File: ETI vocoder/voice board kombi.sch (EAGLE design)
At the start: 94 parts, among them IC1 TL072P, IC2 TL072P, IC3 TL081P, IC4 TL081P, IC5 TL072P, IC6 LM13600AN, IC7 TL072P, Q1 BF244, Q2 BC214

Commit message: Duplicated all parts, ready for creating channel 2 (after main computer bailed on me and I lost a days work)
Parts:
- added C1., C10., C11., C12., C2., C3., C4., C5., C6., C7., C8., C9., CE1., CE2., CE3., CE4.: (no value), resistor:C-EU050-025X075
- added D1., D2., D3., D4.: (no value), diode:DIODE-D-5
- added IC1., IC2., IC7.: TL072P, linear:TL072P
- added IC3., IC4.: TL081P, linear:TL081P
- added PR1., PR2., PR3., PR4., PR5.: (no value), pot:TRIM_EU-CA9V
- added Q1.: BF244, transistor-fet:TN0602N3
- added Q2.: BC214, transistor-pnp:BC214
- added R1., R10., R11., R12., R13., R14., R15., R16., R17., R18., R19., R2., R20., R21., R22., R23., R24., R25., R26., R27., R28., R29., R3., R30., R31., R32., R33., R34., R4., R5., R6., R7., R8., R9., RE1., RE10., RE2., RE3., RE4., RE5., RE6., RE7.: (no value), resistor:R-US_0207/7
- added RV1.: 100k log, joakim:POT16_W_BRACKET""
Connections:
- new net BIAS2: R16..1, R33..1, R34..2
- new net N$47: C1..2, IC1.A.-IN, R2..1, RE3..2
- new net N$48: C1..1, C2..1, PR1..A, R1..2, RE2..1
- new net N$49: C2..2, IC1.A.OUT, R2..2, R3..1
- new net N$50: C3..1, C4..1, R3..2, R4..2, RE4..1
- new net N$51: C3..2, IC1.B.-IN, R5..2
- new net N$52: IC1.B.+IN, R6..2, RE4..2
- new net N$53: C4..2, IC1.B.OUT, R5..1, R7..1
- new net N$54: IC2.B.-IN, R7..2, R8..1, R9..1
- new net N$55: D1..C, IC2.A.+IN, R8..2
- new net N$56: D1..A, D2..C, IC2.B.OUT
- new net N$57: D2..A, R10..1, R9..2
- new net N$58: IC2.A.-IN, R10..2, R11..1
- new net N$59: IC2.A.OUT, R11..2, R12..1
- new net N$60: C5..2, R12..2, R13..1
- new net N$61: C5..1, IC3..-IN, IC3..OUT, R14..1, R15..2
- new net N$62: C6..2, IC3..+IN, R13..2
- new net N$63: Q1..D, R15..1, R16..2
- new net N$64: C7..2, IC4..+IN, Q1..S
- new net N$65: D3..A, Q1..G, R17..2
- new net N$66: IC4..-IN, IC4..OUT, IC5B.+IN, R17..1
- new net N$67: D4..C, IC5B.-IN, R18..1
- new net N$68: D4..A, IC5B.OUT, PR2..E
- new net N$69: PR2..A, PR2..S, Q2..E, R19..1
- new net N$70: PR3..S, R19..2
- new net N$71: Q2..C, R20..2
- new net N$72: PR4..A, R31..2
- new net N$73: C8..2, C9..2, PR5..A, R21..2, RE5..1
- new net N$74: C10..2, C11..2, R23..2, R24..2, RE7..1
- new net N$75: C8..1, IC7.A.-IN, R22..1, RE10..2
- new net N$76: C9..1, IC7.A.OUT, R22..2, R23..1
- new net N$77: C11..1, IC7.B.OUT, R25..2, R27..1
- new net N$78: PR4..E, R32..1
- new net N$79: IC6B.+IN, R32..2
- new net N$80: IC6B.DIODE/BIAS, R28..1
- new net N$81: IC6B.-IN, R27..2, R31..1
- new net N$82: IC6B.AMP/BIAS, R20..1
- new net N$83: IC6B.BUFF/IN, RV1.G$1.1S
- new net N$84: C12..2, IC6B.BUFF/OUT, R29..1
- new net N$85: C12..1, R30..1
- new net N$86: C10..1, IC7.B.-IN, R25..1
- new net N$87: IC7.B.+IN, R26..2, RE7..2
- new net N$88: CE1..2, R1..1, RE1..2
- new net N$89: CE2..2, IC1.A.+IN, RE2..2
- new net N$90: CE3..2, R21..1
- new net N$91: CE4..2, IC7.A.+IN, RE5..2, RE6..2
- new net N$92: IC6B.OUT, RV1.G$1.1E
- net +12V: now also IC1.P.V+, IC2.P.V+, IC3..V+, IC4..V+, IC7.P.V+, PR3..A, R28..2, R33..2
- net -12V: now also IC1.P.V-, IC2.P.V-, IC3..V-, IC4..V-, IC7.P.V-, PR3..E, R29..2
- net EXITATION_IN: now also CE3..1
- net GND: now also C6..1, C7..1, CE2..1, CE4..1, IC2.B.+IN, PR1..E, PR1..S, PR4..S, PR5..E, PR5..S, Q2..B, R18..2, R24..1, R26..1, R34..1, R4..1, R6..1, RE1..1, RE10..1, RE3..1, RE6..1, RV1.G$1.1A
- net OUTPUT_AMP: now also R30..2
- net SLEW_RATE_CTRL: now also D3..C
- net SPEECH_IN: now also CE1..1
- net VU_DETECTOR: now also R14..2
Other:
- moved on the sheet: C12, C5, C6, C7, CE1, CE2, CE3, CE4, D1, D2, D3, D4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

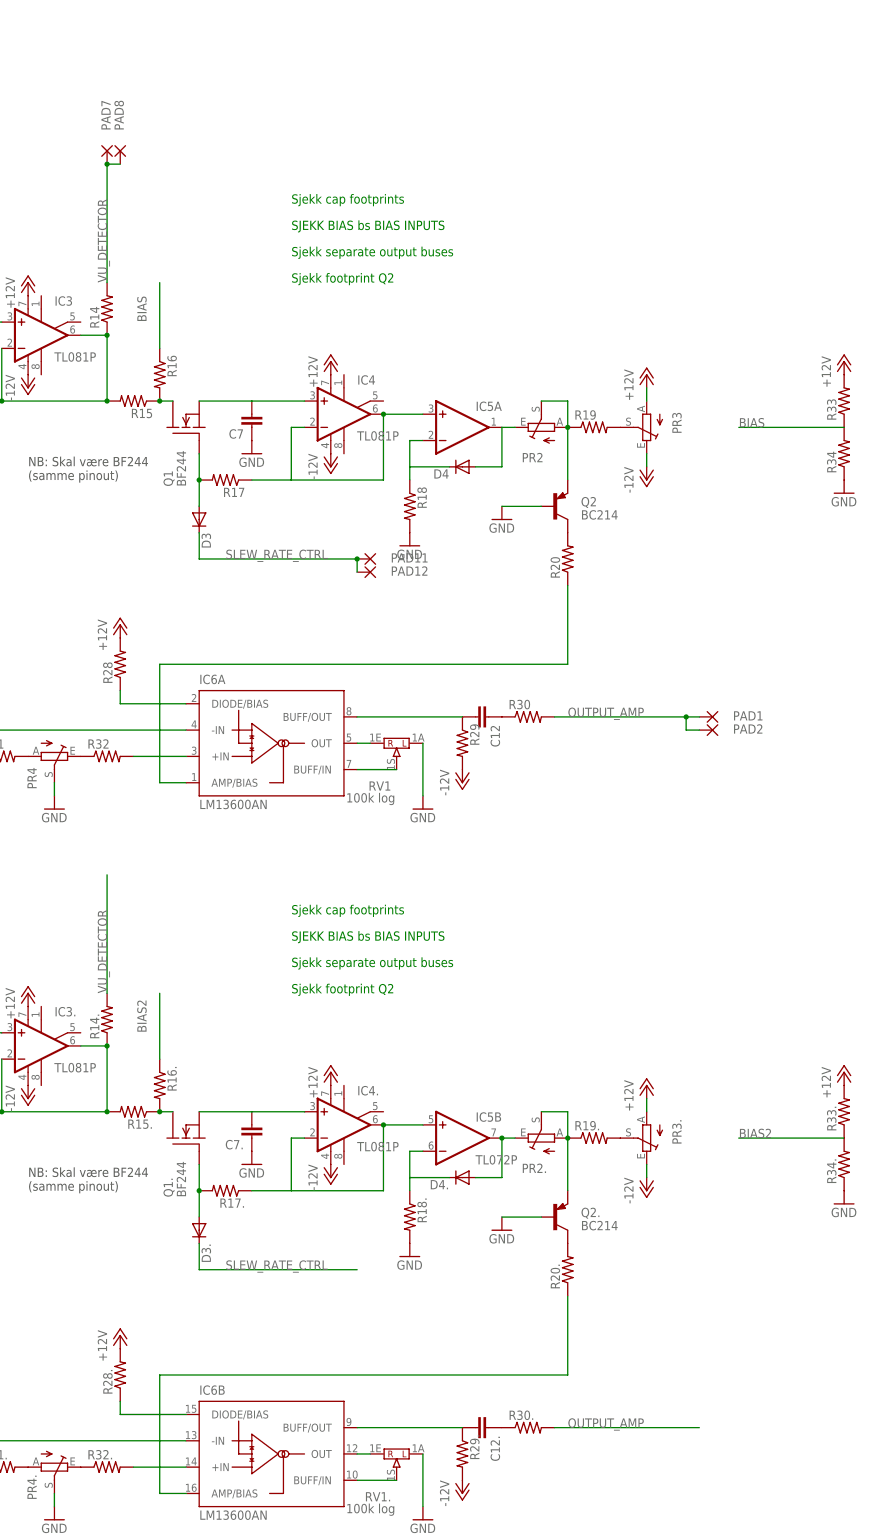
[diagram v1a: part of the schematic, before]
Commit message: Checked and fixed Q2, still need to check cap footprints and shrink board
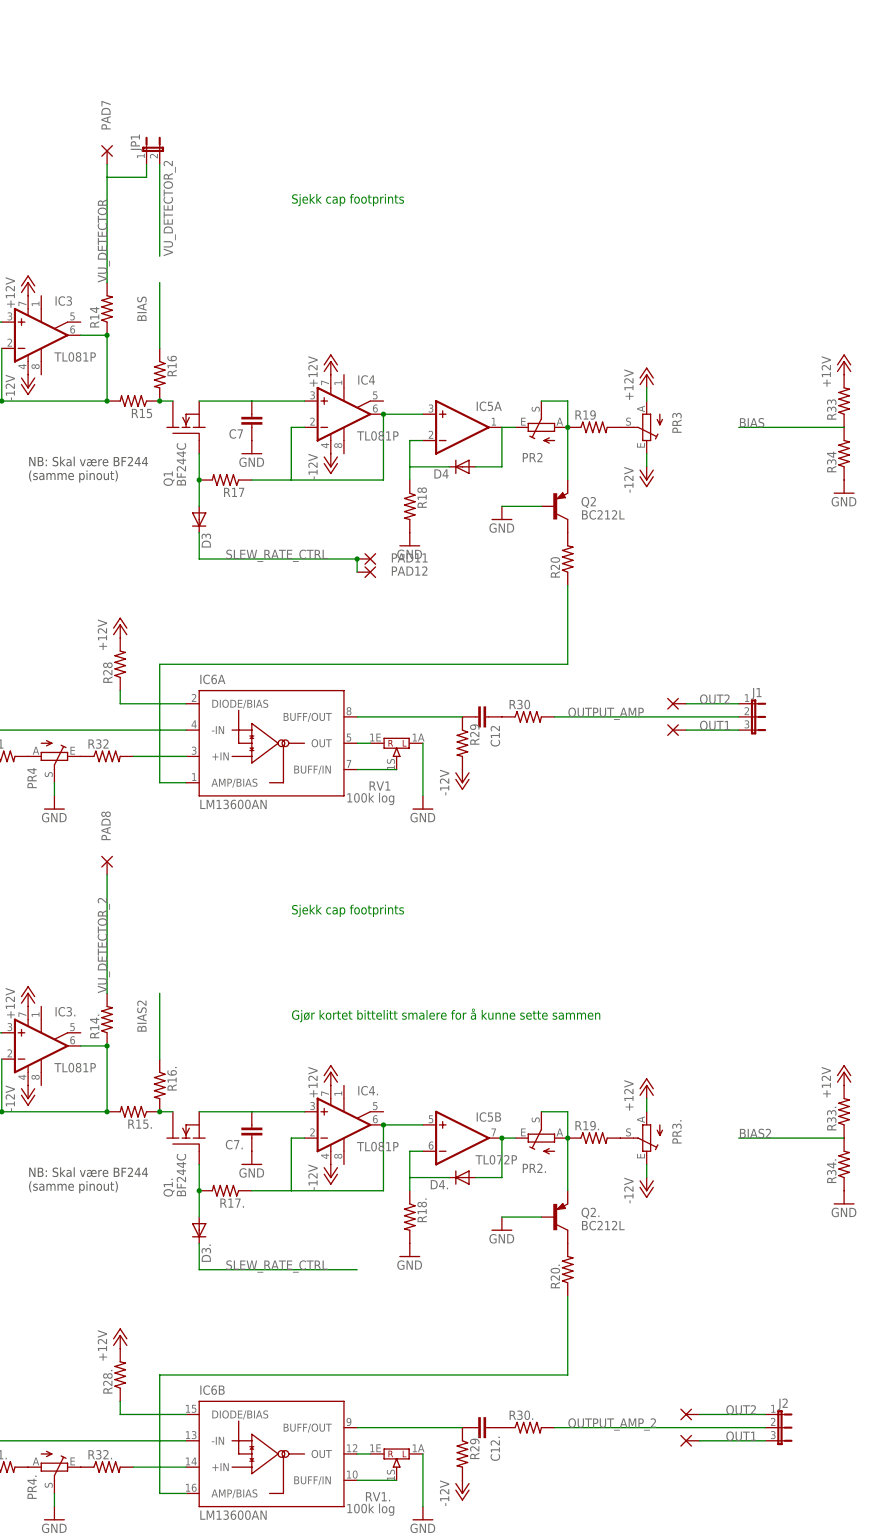
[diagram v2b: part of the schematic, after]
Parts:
- added J1, J2: (no value), jumper:JP2E
- added JP1: (no value), jumper:JP1E
- added PAD17, PAD18: WIREPAD2,54/1,1, wirepad:WIREPAD2,54/1,1
- Q1, Q1.: value BF244 -> BF244C
- Q2, Q2.: value BC214 -> BC212L; device transistor-pnp:BC214 -> transistor-neu-to92:-PNP-TO92-ECB
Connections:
- new net OUT1: J1.3, J2.3, PAD1.P, PAD2.P
- new net OUT2: J1.1, J2.1, PAD17.P, PAD18.P
- new net OUTPUT_AMP_2: J2.2, R30..2
- new net VU_DETECTOR_2: JP1.2, PAD8.P, R14..2
- net OUTPUT_AMP: now also J1.2; no longer PAD1.P, PAD2.P, R30..2
- net VU_DETECTOR: now also JP1.1; no longer PAD8.P, R14..2
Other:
- note added: "Gjør kortet bittelitt smalere for å kunne sette sammen"
- note removed: "SJEKK BIAS bs BIAS INPUTS"
- note removed: "Sjekk footprint Q2"
- note removed: "Sjekk separate output buses"
- moved on the sheet: PAD8
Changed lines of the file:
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@@
 <part name="C6" library="resistor" deviceset="C-EU" device="050-025X075"/>
 <part name="GND5" library="supply1" deviceset="GND" device=""/>
-<part name="Q1" library="transistor-fet" deviceset="TN0602N3" device="" value="BF244"/>
+<part name="Q1" library="transistor-fet" deviceset="TN0602N3" device="" value="BF244C"/>
 <part name="D3" library="diode" deviceset="DIODE-" device="D-5"/>
 <part name="R17" library="resistor" deviceset="R-US_" device="0207/7"/>
@@
 <part name="P+1" library="supply1" deviceset="+12V" device=""/>
 <part name="P-1" library="supply1" deviceset="-12V" device=""/>
-<part name="Q2" library="transistor-pnp" deviceset="BC214" device=""/>
+<part name="Q2" library="transistor-neu-to92" deviceset="*-PNP-" device="TO92-ECB" value="BC212L"/>
 <part name="GND8" library="supply1" deviceset="GND" device=""/>
 <part name="R20" library="resistor" deviceset="R-US_" device="0207/7"/>
@@
 <part name="C6." library="resistor" deviceset="C-EU" device="050-025X075"/>
 <part name="GND27" library="supply1" deviceset="GND" device=""/>
-<part name="Q1." library="transistor-fet" deviceset="TN0602N3" device="" value="BF244"/>
+<part name="Q1." library="transistor-fet" deviceset="TN0602N3" device="" value="BF244C"/>
 <part name="D3." library="diode" deviceset="DIODE-" device="D-5"/>
 <part name="R17." library="resistor" deviceset="R-US_" device="0207/7"/>
@@
 <part name="P+9" library="supply1" deviceset="+12V" device=""/>
 <part name="P-8" library="supply1" deviceset="-12V" device=""/>
-<part name="Q2." library="transistor-pnp" deviceset="BC214" device=""/>
+<part name="Q2." library="transistor-neu-to92" deviceset="*-PNP-" device="TO92-ECB" value="BC212L"/>
 <part name="GND30" library="supply1" deviceset="GND" device=""/>
 <part name="R20." library="resistor" deviceset="R-US_" device="0207/7"/>
@@
 <part name="P-12" library="supply1" deviceset="-12V" device=""/>
 <part name="P+14" library="supply1" deviceset="+12V" device=""/>
+<part name="J1" library="jumper" deviceset="JP2E" device=""/>
+<part name="J2" library="jumper" deviceset="JP2E" device=""/>
+<part name="PAD17" library="wirepad" deviceset="WIREPAD" device="2,54/1,1"/>
+<part name="PAD18" library="wirepad" deviceset="WIREPAD" device="2,54/1,1"/>
+<part name="JP1" library="jumper" deviceset="JP1E" device=""/>
 </parts>
 <sheets>
@@
 H: R24
 L: R24</text>
-<text x="233.68" y="231.14" size="1.778" layer="91">SJEKK BIAS bs BIAS INPUTS</text>
-<text x="233.68" y="226.06" size="1.778" layer="91">Sjekk separate output buses</text>
 <text x="233.68" y="236.22" size="1.778" layer="91">Sjekk cap footprints</text>
-<text x="233.68" y="220.98" size="1.778" layer="91">Sjekk footprint Q2</text>
 <text x="111.76" y="185.42" size="1.778" layer="97">2A and 2B are switched in the article</text>
 <text x="182.88" y="45.72" size="1.778" layer="97">NB: Skal være BF244
@@
 H: R24
 L: R24</text>
-<text x="233.68" y="93.98" size="1.778" layer="91">SJEKK BIAS bs BIAS INPUTS</text>
-<text x="233.68" y="88.9" size="1.778" layer="91">Sjekk separate output buses</text>
 <text x="233.68" y="99.06" size="1.778" layer="91">Sjekk cap footprints</text>
-<text x="233.68" y="83.82" size="1.778" layer="91">Sjekk footprint Q2</text>
 <text x="111.76" y="48.26" size="1.778" layer="97">2A and 2B are switched in the article</text>
+<text x="233.68" y="78.74" size="1.778" layer="91">Gjør kortet bittelitt smalere for å kunne sette sammen</text>
 </plain>
 <instances>
@@
 <instance part="P-6" gate="1" x="114.3" y="238.76"/>
 <instance part="P+7" gate="1" x="114.3" y="259.08"/>
-<instance part="PAD1" gate="G$1" x="314.96" y="137.16" smashed="yes" rot="R180">
-<attribute name="NAME" x="318.897" y="136.4742" size="1.778" layer="95"/>
-</instance>
-<instance part="PAD2" gate="G$1" x="314.96" y="134.62" smashed="yes" rot="R180">
-<attribute name="NAME" x="318.897" y="133.9342" size="1.778" layer="95"/>
-</instance>
+<instance part="PAD1" gate="G$1" x="307.34" y="134.62" smashed="yes"/>
+<instance part="PAD2" gate="G$1" x="309.88" y="-2.54" smashed="yes"/>
 <instance part="PAD3" gate="G$1" x="33.02" y="137.16" smashed="yes">
 <attribute name="NAME" x="29.083" y="137.8458" size="1.778" layer="95" rot="R180"/>
@@
 <attribute name="NAME" x="198.8058" y="250.317" size="1.778" layer="95" rot="R90"/>
 </instance>
-<instance part="PAD8" gate="G$1" x="200.66" y="246.38" smashed="yes" rot="R270">
-<attribute name="NAME" x="201.3458" y="250.317" size="1.778" layer="95" rot="R90"/>
+<instance part="PAD8" gate="G$1" x="198.12" y="109.22" smashed="yes" rot="R270">
+<attribute name="NAME" x="198.8058" y="113.157" size="1.778" layer="95" rot="R90"/>
 </instance>
 <instance part="PAD11" gate="G$1" x="248.92" y="167.64" smashed="yes" rot="R180">
@@
 <instance part="P+14" gate="1" x="114.3" y="114.3"/>
 <instance part="IC5" gate="B" x="266.7" y="55.88"/>
+<instance part="J1" gate="1" x="322.58" y="137.16" rot="R270"/>
+<instance part="J2" gate="1" x="327.66" y="0" rot="R270"/>
+<instance part="PAD17" gate="G$1" x="307.34" y="139.7" smashed="yes"/>
+<instance part="PAD18" gate="G$1" x="309.88" y="2.54" smashed="yes"/>
+<instance part="JP1" gate="A" x="205.74" y="246.38"/>
 </instances>
 <busses>
@@
 <segment>
 <pinref part="R14" gate="G$1" pin="2"/>
-<wire x1="198.12" y1="220.98" x2="198.12" y2="243.84" width="0.1524" layer="91"/>
+<wire x1="198.12" y1="220.98" x2="198.12" y2="241.3" width="0.1524" layer="91"/>
 <label x="198.12" y="220.98" size="1.778" layer="95" rot="R90"/>
-<pinref part="PAD8" gate="G$1" pin="P"/>
 <pinref part="PAD7" gate="G$1" pin="P"/>
-<wire x1="200.66" y1="243.84" x2="198.12" y2="243.84" width="0.1524" layer="91"/>
-<junction x="198.12" y="243.84"/>
-</segment>
-<segment>
-<pinref part="R14." gate="G$1" pin="2"/>
-<wire x1="198.12" y1="83.82" x2="198.12" y2="106.68" width="0.1524" layer="91"/>
-<label x="198.12" y="83.82" size="1.778" layer="95" rot="R90"/>
+<wire x1="198.12" y1="241.3" x2="198.12" y2="243.84" width="0.1524" layer="91"/>
+<wire x1="198.12" y1="241.3" x2="205.74" y2="241.3" width="0.1524" layer="91"/>
+<pinref part="JP1" gate="A" pin="1"/>
+<wire x1="205.74" y1="241.3" x2="205.74" y2="243.84" width="0.1524" layer="91"/>
 </segment>
 </net>
@@
 <segment>
 <pinref part="R30" gate="G$1" pin="2"/>
-<wire x1="284.48" y1="137.16" x2="309.88" y2="137.16" width="0.1524" layer="91"/>
+<wire x1="284.48" y1="137.16" x2="320.04" y2="137.16" width="0.1524" layer="91"/>
 <label x="287.02" y="137.16" size="1.778" layer="95"/>
-<pinref part="PAD1" gate="G$1" pin="P"/>
-<pinref part="PAD2" gate="G$1" pin="P"/>
-<wire x1="309.88" y1="137.16" x2="312.42" y2="137.16" width="0.1524" layer="91"/>
-<wire x1="312.42" y1="134.62" x2="309.88" y2="134.62" width="0.1524" layer="91"/>
-<wire x1="309.88" y1="134.62" x2="309.88" y2="137.16" width="0.1524" layer="91"/>
-<junction x="309.88" y="137.16"/>
-</segment>
-<segment>
-<pinref part="R30." gate="G$1" pin="2"/>
-<wire x1="284.48" y1="0" x2="312.42" y2="0" width="0.1524" layer="91"/>
-<label x="287.02" y="0" size="1.778" layer="95"/>
+<pinref part="J1" gate="1" pin="2"/>
 </segment>
 </net>
@@
 </segment>
 </net>
+<net name="OUT1" class="0">
+<segment>
+<pinref part="J2" gate="1" pin="3"/>
+<pinref part="PAD2" gate="G$1" pin="P"/>
+<wire x1="312.42" y1="-2.54" x2="325.12" y2="-2.54" width="0.1524" layer="91"/>
+<label x="317.5" y="-2.54" size="1.778" layer="95"/>
+</segment>
+<segment>
+<pinref part="J1" gate="1" pin="3"/>
+<pinref part="PAD1" gate="G$1" pin="P"/>
+<wire x1="309.88" y1="134.62" x2="320.04" y2="134.62" width="0.1524" layer="91"/>
+<label x="312.42" y="134.62" size="1.778" layer="95"/>
+</segment>
+</net>
+<net name="OUT2" class="0">
+<segment>
+<pinref part="J2" gate="1" pin="1"/>
+<pinref part="PAD18" gate="G$1" pin="P"/>
+<wire x1="312.42" y1="2.54" x2="325.12" y2="2.54" width="0.1524" layer="91"/>
+<label x="317.5" y="2.54" size="1.778" layer="95"/>
+</segment>
+<segment>
+<pinref part="J1" gate="1" pin="1"/>
+<pinref part="PAD17" gate="G$1" pin="P"/>
+<wire x1="309.88" y1="139.7" x2="320.04" y2="139.7" width="0.1524" layer="91"/>
+<label x="312.42" y="139.7" size="1.778" layer="95"/>
+</segment>
+</net>
+<net name="OUTPUT_AMP_2" class="0">
+<segment>
+<pinref part="R30." gate="G$1" pin="2"/>
+<wire x1="284.48" y1="0" x2="325.12" y2="0" width="0.1524" layer="91"/>
+<label x="287.02" y="0" size="1.778" layer="95"/>
+<pinref part="J2" gate="1" pin="2"/>
+</segment>
+</net>
+<net name="VU_DETECTOR_2" class="0">
+<segment>
+<pinref part="R14." gate="G$1" pin="2"/>
+<wire x1="198.12" y1="83.82" x2="198.12" y2="106.68" width="0.1524" layer="91"/>
+<label x="198.12" y="83.82" size="1.778" layer="95" rot="R90"/>
+<pinref part="PAD8" gate="G$1" pin="P"/>
+</segment>
+<segment>
+<pinref part="JP1" gate="A" pin="2"/>
+<wire x1="208.28" y1="243.84" x2="208.28" y2="226.06" width="0.1524" layer="91"/>
+<label x="210.82" y="226.06" size="1.778" layer="95" rot="R90"/>
+</segment>
+</net>

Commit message: Switched to dual footprint caps for all caps (5mm, 7.5mm). Added footprint to custom library
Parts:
- C1, C1., C10, C10., C11, C11., C12, C12., C2, C2., C3, C3., C4, C4., C5, C5., C6, C6., C7, C7., C8, C8., C9, C9., CE1, CE1., CE2, CE2., CE3, CE3., CE4, CE4.: device resistor:C-EU050-025X075 -> joakim:C-EU050_075-025X100
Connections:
- net GND: now also C7..2, C7.2; no longer C7..1, C7.1
- net N$18: now also C7.1; no longer C7.2
- net N$43: now also CE1.1; no longer CE1.2
- net N$64: now also C7..1; no longer C7..2
- net N$88: now also CE1..1; no longer CE1..2
- net SPEECH_IN: now also CE1..2, CE1.2; no longer CE1..1, CE1.1
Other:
- moved on the sheet: C7, C7., CE1, CE1., CE3

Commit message: Replaced all c/r combinations with special component
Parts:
- C1, C1., C10, C10., C3, C3., C8, CE2, CE2., CE4, CE4.: value (none) -> C-OR-R050_075-025X100; device joakim:C-EU050_075-025X100 -> joakim:C-OR-R050_075-025X100
- R1, R1., R23, R23., R26, R26., R3, R3., R6, R6., RE2, RE2., RE4, RE4., RE5, RE5., RE7, RE7.: value (none) -> C-OR-R050_075-025X100; device resistor:R-US_0207/7 -> joakim:C-OR-R050_075-025X100
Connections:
- net N$2: now also R1.1; no longer R1.2
- net N$43: now also R1.2; no longer R1.1
- net N$48: now also R1..1; no longer R1..2
- net N$88: now also R1..2; no longer R1..1
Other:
- note added: "B: R21 H: short L: R21"
- note added: "B: short H: C8 L: C14"
- note added: "Error in parts list, should be BF244C"
- note added: "Sjekk om denne skal være elektrolytt"
- note added: "rename shared"
- note added: "snu samme vei?"
- note removed: "B: R21 H: C8 L: R21"
- note removed: "B: short H: short L: C14"
- note removed: "Gjør kortet bittelitt smalere for å kunne sette sammen"
- note removed: "NB: Skal være BF244 (samme pinout)"
- moved on the sheet: CE3
